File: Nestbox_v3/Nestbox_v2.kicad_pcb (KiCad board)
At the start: 2 copper layers, 85 x 60 mm, 102 parts, among them J201 BATT_CONN_01X02, J301 CONN_01X04, J402 CONN_01X05, J502 CONN_01X06, J601 LOAD_CELL_CONN_01X04, J701 RFID_CONN_01X05, P301 RX/TX, P302 TST/RST, P303 DEBUG_3V3, Q201 TPH1R712MDL1Q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

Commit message: reworked silk layer for PCBA. generated position files. reviewed parts MPN for final order
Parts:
- moved G*** 54.4 mm to (23.0, -9.00), turned to 180 degrees
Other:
- board text added: "Digital Nestbox v3.1 by"
- board text removed: "Digital Nestbox v3.0 by"
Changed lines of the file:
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@@
     (links 223)
     (no_connects 1)
-    (area -7.600001 -57.600001 77.600001 2.600001)
+    (area -42.849999 -82.95 95.35 8.700001)
     (thickness 1.6)
-    (drawings 61)
+    (drawings 84)
     (tracks 1349)
     (zones 0)
@@
     (34 B.Paste user)
     (35 F.Paste user)
-    (36 B.SilkS user hide)
+    (36 B.SilkS user)
     (37 F.SilkS user)
     (38 B.Mask user)
@@
     (pad_to_mask_clearance 0.2)
     (aux_axis_origin 0 0)
-    (visible_elements FFFEFF3F)
+    (grid_origin -7.5 2.5)
+    (visible_elements FFFEFF7F)
     (pcbplotparams
       (layerselection 0x010fc_80000001)
@@
     (at 73.24 -41.155 270)
     (attr smd)
-    (fp_text reference D301 (at -0.35 -1.72 450) (layer B.SilkS) hide
+    (fp_text reference D301 (at 3.905 -0.01 450) (layer B.SilkS)
       (effects (font (size 0.889 0.889) (thickness 0.1016)) (justify mirror))
     )
@@
     (at 71.24 -41.155 270)
     (attr smd)
-    (fp_text reference D302 (at -0.35 1.78 450) (layer B.SilkS) hide
+    (fp_text reference D302 (at 3.905 -0.01 450) (layer B.SilkS)
       (effects (font (size 0.889 0.889) (thickness 0.1016)) (justify mirror))
     )
@@
     (at 66.69 -13.855 270)
     (descr "2-way 3.5mm pitch terminal block, Phoenix PT series")
-    (fp_text reference J201 (at -3.15 -0.02 360) (layer B.SilkS)
+    (fp_text reference J201 (at -3.15 -0.02 360) (layer B.SilkS) hide
       (effects (font (size 1 1) (thickness 0.15)) (justify mirror))
     )
@@
     (tags "SSOP 0.65")
     (attr smd)
-    (fp_text reference U601 (at 0 -3.55 270) (layer F.SilkS)
+    (fp_text reference U601 (at -6.31 -0.205 360) (layer F.SilkS)
       (effects (font (size 1 1) (thickness 0.15)))
     )
@@
     (at 28.58 -42.76 180)
     (descr "5-way 2.54mm pitch terminal block, Phoenix MPT series")
-    (fp_text reference J402 (at 5.08 4.50088 180) (layer B.SilkS)
+    (fp_text reference J402 (at 5.08 4.50088 180) (layer B.SilkS) hide
       (effects (font (size 1 1) (thickness 0.15)) (justify mirror))
     )
@@
     (at 8.48 -22.5 270)
     (descr "4-way 2.54mm pitch terminal block, Phoenix MPT series")
-    (fp_text reference J601 (at 9.79 -0.515 540) (layer B.SilkS)
+    (fp_text reference J601 (at 9.79 -0.515 360) (layer B.SilkS) hide
       (effects (font (size 1 1) (thickness 0.15)) (justify mirror))
     )
@@
     (at 8.44 -41.3 270)
     (descr "5-way 2.54mm pitch terminal block, Phoenix MPT series")
-    (fp_text reference J701 (at 5.08 4.50088 270) (layer B.SilkS)
+    (fp_text reference J701 (at 5.08 4.50088 270) (layer B.SilkS) hide
       (effects (font (size 1 1) (thickness 0.15)) (justify mirror))
     )
@@
   )
   (module Octanis3:octanis3_logo locked (layer B.Cu)
-    (at 70.21 -36.005 90)
+    (at 23 -9 180)
     (attr smd)
-    (fp_text reference G*** (at 0 0 90) (layer B.SilkS) hide
+    (fp_text reference G*** (at 0 0 180) (layer B.SilkS) hide
       (effects (font (thickness 0.3)) (justify mirror))
     )
-    (fp_text value LOGO (at 0.75 0 90) (layer B.SilkS) hide
+    (fp_text value LOGO (at 0.75 0 180) (layer B.SilkS) hide
       (effects (font (thickness 0.3)) (justify mirror))
     )
@@
     (descr "Through hole straight socket strip, 1x01, 2.00mm pitch, single row")
     (tags "Through hole socket strip THT 1x01 2.00mm single row")
-    (fp_text reference TP_RTC301 (at -5.75 0) (layer F.SilkS)
+    (fp_text reference TP_RTC301 (at -5.75 0) (layer F.SilkS) hide
       (effects (font (size 1 1) (thickness 0.15)))
     )
@@
       (net 3 VAA))
   )
+  (gr_line (start 71.25 -46) (end 71.25 -44.75) (layer B.SilkS) (width 0.2))
+  (gr_line (start 70.75 -44.75) (end 71.75 -44.75) (layer B.SilkS) (width 0.2))
+  (gr_line (start 71.25 -44.75) (end 70.75 -44.75) (layer B.SilkS) (width 0.2))
+  (gr_line (start 71.75 -45.25) (end 71.25 -44.75) (layer B.SilkS) (width 0.2))
+  (gr_line (start 70.75 -45.25) (end 71.75 -45.25) (layer B.SilkS) (width 0.2))
+  (gr_line (start 71.25 -44.75) (end 70.75 -45.25) (layer B.SilkS) (width 0.2))
+  (gr_line (start 71.75 -44.75) (end 71.25 -44.75) (layer B.SilkS) (width 0.2))
+  (gr_line (start 71.25 -44.75) (end 71.25 -43.75) (layer B.SilkS) (width 0.2))
+  (gr_line (start 73.25 -44.75) (end 73.25 -43.75) (layer B.SilkS) (width 0.2))
+  (gr_line (start 73.75 -44.75) (end 73.25 -44.75) (layer B.SilkS) (width 0.2))
+  (gr_line (start 72.75 -44.75) (end 73.75 -44.75) (layer B.SilkS) (width 0.2))
+  (gr_line (start 73.25 -44.75) (end 72.75 -44.75) (layer B.SilkS) (width 0.2))
+  (gr_line (start 73.75 -45.25) (end 73.25 -44.75) (layer B.SilkS) (width 0.2))
+  (gr_line (start 72.75 -45.25) (end 73.75 -45.25) (layer B.SilkS) (width 0.2))
+  (gr_line (start 73.25 -44.75) (end 72.75 -45.25) (layer B.SilkS) (width 0.2))
+  (gr_line (start 73.25 -46) (end 73.25 -44.75) (layer B.SilkS) (width 0.2))
+  (gr_text . (at 25.5 -3.5 90) (layer F.SilkS)
+    (effects (font (size 2 2) (thickness 0.5)))
+  )
+  (gr_text . (at 70 -9.75 90) (layer F.SilkS)
+    (effects (font (size 2 2) (thickness 0.5)))
+  )
+  (gr_text . (at 71.75 -21.5 90) (layer F.SilkS)
+    (effects (font (size 2 2) (thickness 0.5)))
+  )
+  (gr_text . (at 66.4638 -45.9558 90) (layer F.SilkS)
+    (effects (font (size 2 2) (thickness 0.5)))
+  )
+  (gr_text . (at 34 -48.75 90) (layer F.SilkS)
+    (effects (font (size 2 2) (thickness 0.5)))
+  )
+  (gr_text . (at 51.75 -21.5 90) (layer F.SilkS)
+    (effects (font (size 2 2) (thickness 0.5)))
+  )
+  (gr_line (start 43 -10) (end 43 -5) (layer F.SilkS) (width 0.4))
   (gr_text "G 3V rx tx\n" (at 37.5 -2.75) (layer B.SilkS)
     (effects (font (size 1 1) (thickness 0.25)) (justify mirror))
@@
   )
   (gr_text . (at 23.495 -22.21 90) (layer F.SilkS)
-    (effects (font (size 1.5 1.5) (thickness 0.3)))
+    (effects (font (size 2 2) (thickness 0.5)))
   )
   (gr_text . (at 67.21 -46.505) (layer F.SilkS)
@@
     (effects (font (size 1.2 1.2) (thickness 0.3) italic) (justify left mirror))
   )
-  (gr_text "data\n" (at 69.21 -42.505 270) (layer B.SilkS)
+  (gr_text "data\n" (at 69.25 -39 270) (layer B.SilkS)
     (effects (font (size 1.2 1.2) (thickness 0.3) italic) (justify left mirror))
   )
-  (gr_text status (at 75.21 -41.505 270) (layer B.SilkS)
+  (gr_text status (at 75.25 -38.25 270) (layer B.SilkS)
     (effects (font (size 1.2 1.2) (thickness 0.3) italic) (justify left mirror))
   )
-  (gr_text "Digital Nestbox v3.0 by" (at 57.71 -32.005 270) (layer B.SilkS)
+  (gr_text "Digital Nestbox v3.1 by" (at 57.71 -32.005 270) (layer B.SilkS)
     (effects (font (size 1.2 1.2) (thickness 0.3) italic) (justify mirror))
   )

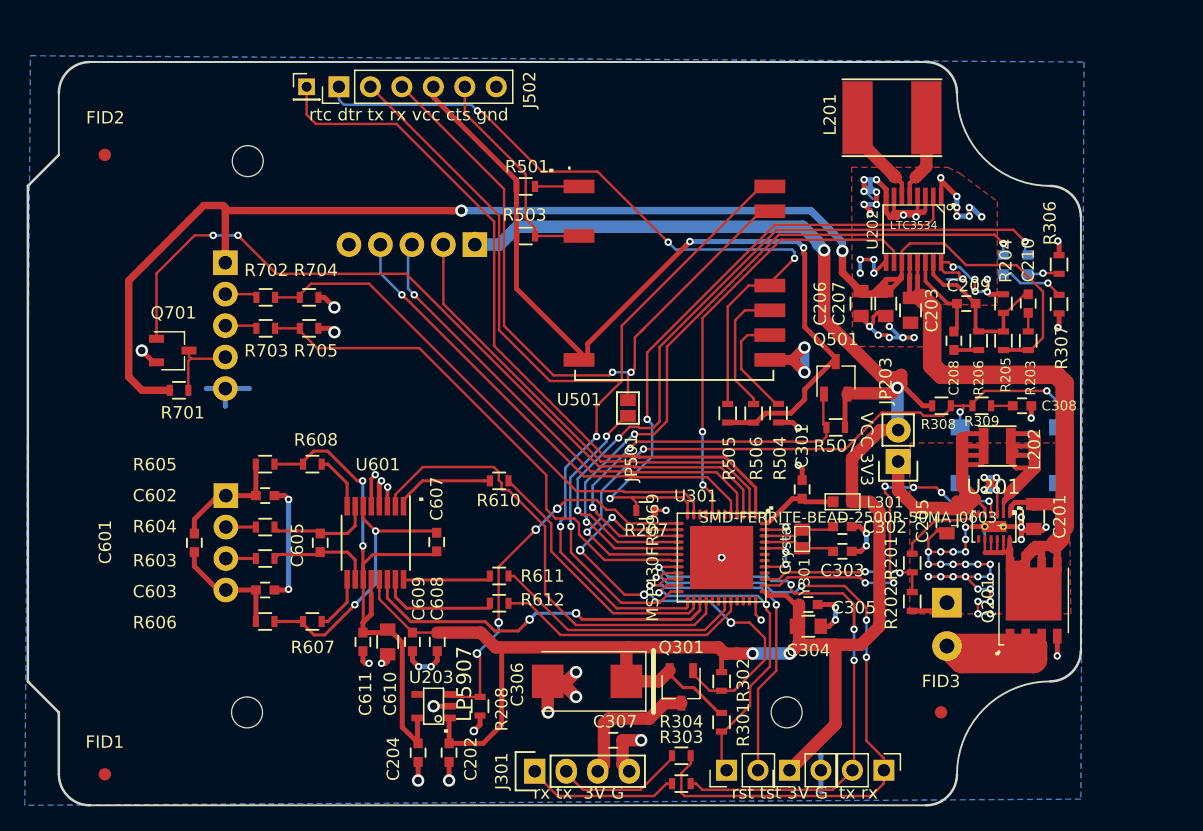
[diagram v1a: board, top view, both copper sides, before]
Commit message: production status nestbox v3
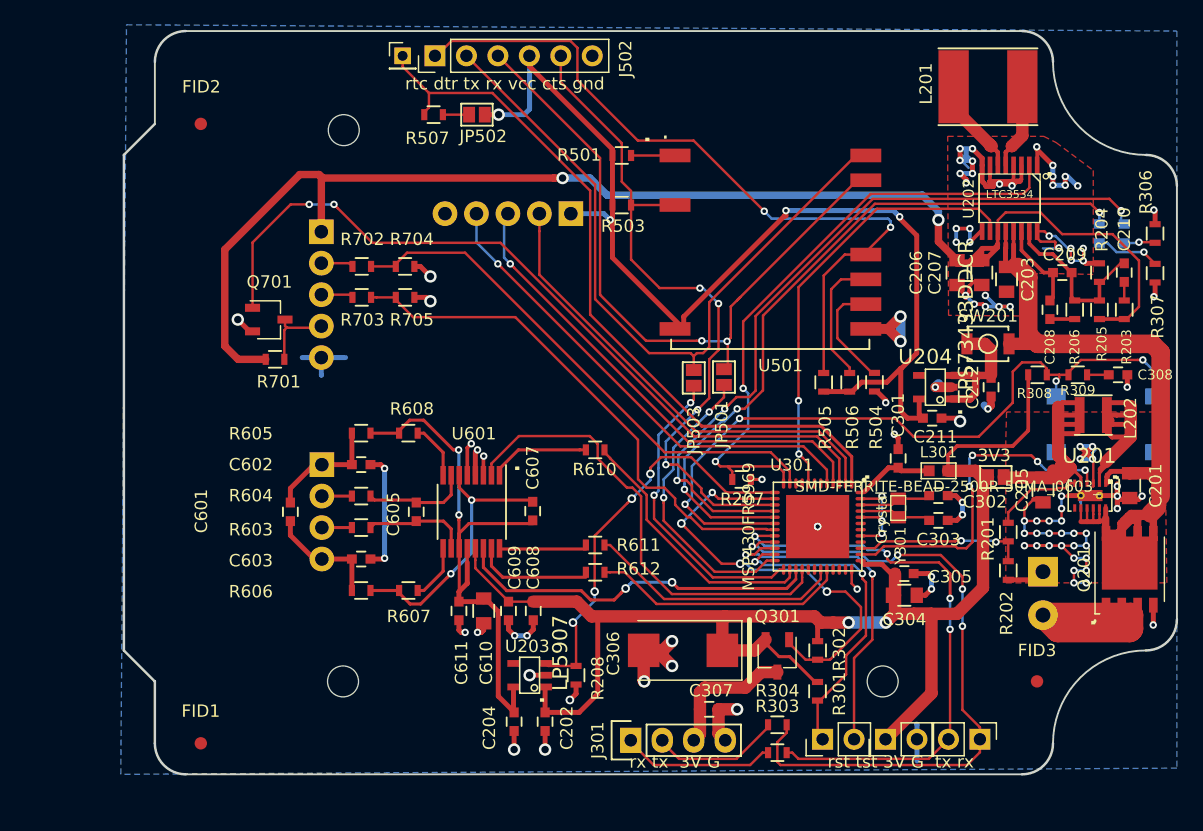
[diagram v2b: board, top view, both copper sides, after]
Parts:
- removed Q501: NTR3A052PZT1G, TO_SOT_Packages_SMD:TSOT-23
- added C211: 2.2u, Capacitors_SMD:C_0603, F.Cu at (65.5, -28.8)
- added C212: 1u, Capacitors_SMD:C_0603, F.Cu at (70.2, -31.2)
- added JP502: Jumper, Connect:GS2, F.Cu at (28.8, -53.2)
- added JP503: Jumper, Connect:GS2, F.Cu at (46.2, -32.0)
- added SW201: external_button, Buttons_Switches_SMD:SW_SPST_B3U-1000P, F.Cu at (70.0, -34.8)
- added U204: TPS73433DDCR, texasinstruments:SOT23-5, F.Cu at (65.8, -31.2)
- C302, C303: value 24p -> 25p
- JP203: footprint Pin_Headers:Pin_Header_Straight_1x02 -> Connect:GS2
- moved R507 41.1 mm to (25.2, -53.2)
- moved C602 8.14 mm to (19.4, -25.0)
- moved C603 8.14 mm to (19.4, -17.4)
- moved G*** 8.14 mm to (43.6, -33.5)
- moved G*** 8.14 mm to (58.5, -33.5)
- moved J701 8.14 mm to (16.2, -43.8)
- moved R603 8.14 mm to (19.4, -19.9)
- moved R604 8.14 mm to (19.4, -22.5)
- moved R605 8.14 mm to (19.4, -27.5)
- moved R606 8.14 mm to (19.4, -14.8)
- moved REF** 8.14 mm to (17.9, -7.50)
- moved C201 8.14 mm to (81.4, -23.3)
- moved C202 8.14 mm to (34.2, -4.25)
- moved C203 8.14 mm to (71.5, -40.0)
- moved C204 8.14 mm to (31.8, -4.25)
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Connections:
- J402 pad 1: +3V3 -> VDDA
- J502 pad 2: /Communication/ESP12_TX -> /Communication/TX
- J502 pad 4: /Communication/ESP12_VCC -> VDDA
- J502 pad 5: /Communication/CTS -> /Communication/ESP12_ENABLE
- R501 pad 1: /Communication/ESP12_VCC -> VDDA
- R503 pad 1: /Communication/ESP12_VCC -> /Communication/ESP12_ENABLE
- R503 pad 2: /Communication/CTS -> VDDA
- R505 pad 1: /Communication/ESP12_VCC -> VDDA
- R506 pad 1: /Communication/ESP12_VCC -> VDDA
- R507 pad 1: +3V3 -> Net-(JP502-Pad2)
- R507 pad 2: /Communication/ESP12_ENABLE -> /Communication/ESP12_VCC_sense
- TP_RTC301 pad 1: /Control/RTC_CAL -> /Communication/ESP12_VCC_sense
- U301 pad 1: /Control/RTC_CAL -> /Communication/ESP12_VCC_sense
- U501 pad 16: /Communication/ESP12_TX -> /Communication/TX
- U501 pad 3: /Communication/CTS -> /Communication/ESP12_ENABLE
- U501 pad 8: /Communication/ESP12_VCC -> VDDA
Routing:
- net VDDA: track 0.00 -> 89.5 mm, vias 0 -> 4
- net /Communication/ESP12_VCC: track 71.0 -> 0.00 mm, vias 2 -> 0
- net /Communication/ESP12_VCC_sense: track 0.00 -> 60.1 mm
- net /Communication/ESP12_TX: track 84.5 -> 24.7 mm
- net /Control/RTC_CAL: track 59.0 -> 0.00 mm
- net /Communication/TX: track 0.00 -> 56.9 mm
- net +3V3: track 174.2 -> 119.6 mm, vias 4 -> 2
- net /Communication/ESP12_ENABLE: track 33.8 -> 56.7 mm, vias 2 -> 4
- net /Communication/CTS: track 18.6 -> 0.00 mm
- net Net-(C212-Pad1): track 0.00 -> 11.1 mm
- net GND: track 202.1 -> 206.5 mm, vias 103 -> 106
- net /Control/DBG_Switch: track 56.9 -> 60.2 mm
- net Net-(C205-Pad1): track 28.1 -> 24.7 mm
- net +BATT: track 71.5 -> 73.8 mm
- net Net-(JP502-Pad2): track 0.00 -> 2.11 mm
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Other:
- board text added: "3V3"
- board text removed: "VCC 3V3"
